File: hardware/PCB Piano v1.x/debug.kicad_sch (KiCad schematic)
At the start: 2 parts, among them J2 1x5 Pin Header, J7 Conn_02x10_Odd_Even

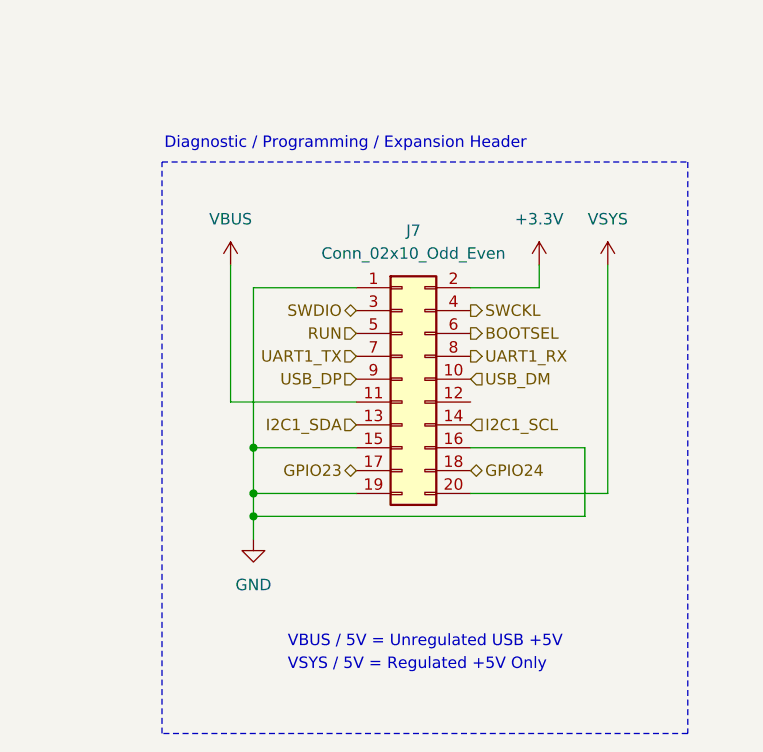
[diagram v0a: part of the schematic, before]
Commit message: Development Phase Update
PCB layout refined more, still not complete. Trying to start a separate v1.1 PCB file to explore a 4-layer PCB.
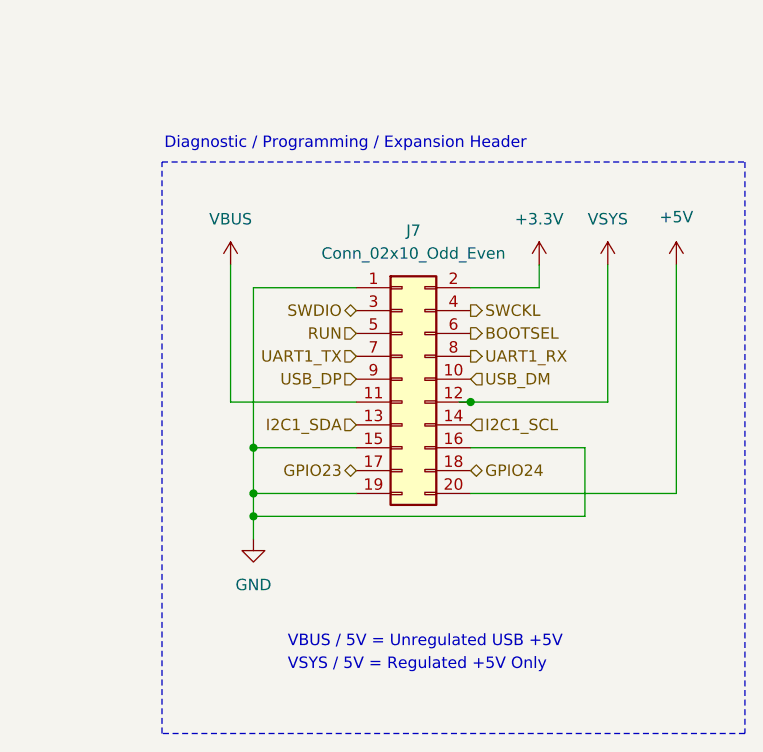
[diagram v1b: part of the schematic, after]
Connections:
- net VSYS: now also J7.12 (Pin_12); no longer J7.20 (Pin_20)
- new net +5V: J7.20 (Pin_20)
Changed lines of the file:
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@@
 	(rectangle
 		(start 144.78 53.34)
-		(end 203.2 116.84)
+		(end 209.55 116.84)
 		(stroke
 			(width 0)
@@
 			(justify left bottom)
 		)
+	)
+	(junction
+		(at 179.07 80.01)
+		(diameter 0)
+		(color 0 0 0 0)
 	)
 	(junction
@@
 	(wire
 		(pts
+			(xy 179.07 90.17) (xy 201.93 90.17)
+		)
+		(stroke
+			(width 0)
+			(type default)
+		)
+	)
+	(wire
+		(pts
 			(xy 40.64 46.99) (xy 50.8 46.99)
 		)
@@
 	(wire
 		(pts
-			(xy 194.31 90.17) (xy 194.31 64.77)
-		)
-		(stroke
-			(width 0)
-			(type default)
-		)
-	)
-	(wire
-		(pts
 			(xy 166.37 80.01) (xy 152.4 80.01)
 		)
@@
 	(wire
 		(pts
-			(xy 179.07 90.17) (xy 194.31 90.17)
-		)
-		(stroke
-			(width 0)
-			(type default)
-		)
-	)
-	(wire
-		(pts
 			(xy 154.94 67.31) (xy 154.94 85.09)
 		)
@@
 	(wire
 		(pts
+			(xy 179.07 80.01) (xy 194.31 80.01)
+		)
+		(stroke
+			(width 0)
+			(type default)
+		)
+	)
+	(wire
+		(pts
+			(xy 201.93 90.17) (xy 201.93 64.77)
+		)
+		(stroke
+			(width 0)
+			(type default)
+		)
+	)
+	(wire
+		(pts
 			(xy 154.94 85.09) (xy 166.37 85.09)
 		)
@@
 	(wire
 		(pts
+			(xy 177.8 80.01) (xy 179.07 80.01)
+		)
+		(stroke
+			(width 0)
+			(type default)
+		)
+	)
+	(wire
+		(pts
 			(xy 179.07 67.31) (xy 186.69 67.31)
 		)
@@
 		(pts
 			(xy 191.77 85.09) (xy 191.77 92.71)
+		)
+		(stroke
+			(width 0)
+			(type default)
+		)
+	)
+	(wire
+		(pts
+			(xy 194.31 80.01) (xy 194.31 64.77)
 		)
 		(stroke
@@
 					(unit 1)
 				)
+			)
+		)
+	)
+	(symbol
+		(lib_id "power:+5V")
+		(at 201.93 64.77 0)
+		(unit 1)
+		(body_style 1)
+		(exclude_from_sim no)
+		(in_bom yes)
+		(on_board yes)
+		(in_pos_files yes)
+		(dnp no)
+		(property "Reference" "#PWR064"
+			(at 201.93 68.58 0)
+			(hide yes)
+			(show_name no)
+			(do_not_autoplace no)
+			(effects
+				(font
+					(size 1.27 1.27)
+				)
+			)
+		)
+		(property "Value" "+5V"
+			(at 201.93 60.198 0)
+			(show_name no)
+			(do_not_autoplace no)
+			(effects
+				(font
+					(size 1.27 1.27)
+				)
+				(justify bottom)
+			)
+		)
+		(property "Footprint" ""
+			(at 201.93 64.77 0)
+			(hide yes)
+			(show_name no)
+			(do_not_autoplace no)
+			(effects
+				(font
+					(size 1.27 1.27)
+				)
+			)
+		)
+		(property "Datasheet" ""
+			(at 201.93 64.77 0)
+			(hide yes)
+			(show_name no)
+			(do_not_autoplace no)
+			(effects
+				(font
+					(size 1.27 1.27)
+				)
+			)
+		)
+		(property "Description" "Power symbol creates a global label with name \"+5V\""
+			(at 201.93 64.77 0)
+			(hide yes)
+			(show_name no)
+			(do_not_autoplace no)
+			(effects
+				(font
+					(size 1.27 1.27)
+				)
+			)
+		)
+		(pin "1"
+		)
+		(instances
+			(project "PCB Piano v1.0"
+				(path "/b31af04b-7e9c-4c59-b32e-b8589263a36a/78fdac94-d1fc-4322-abb1-82836233b440"
+					(reference "#PWR064")
+					(unit 1)
+				)
